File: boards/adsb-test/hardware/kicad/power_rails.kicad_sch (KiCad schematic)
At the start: 57 parts, among them SW401 POWER (slide), U411 TPS62933, U421 TPS62933, U430 TPS22917, U431 TPS22917, U432 TPS22917, U433 TPS22917

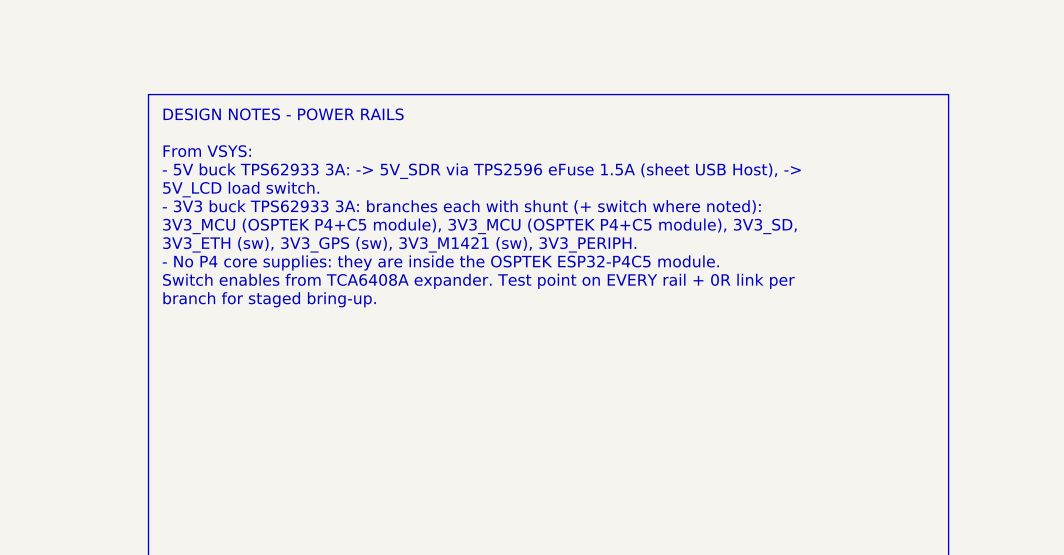
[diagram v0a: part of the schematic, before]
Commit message: ADSB_Test: net classes + diff-pair rules, USB pairs renamed _D_P/_D_N, U201 VSYS drawn at the bottom
Co-Authored-By: Claude Opus 5.5 <noreply@anthropic.com>
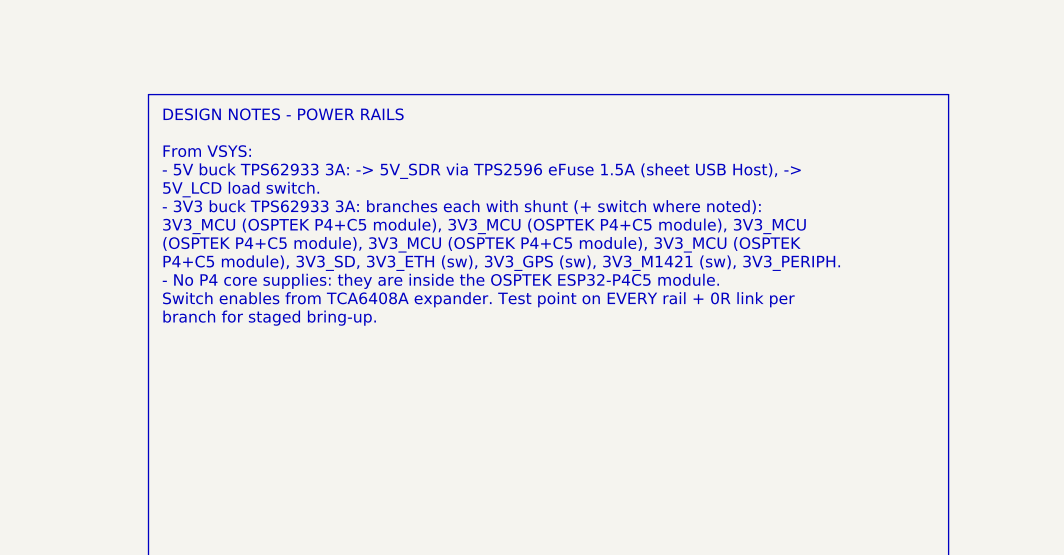
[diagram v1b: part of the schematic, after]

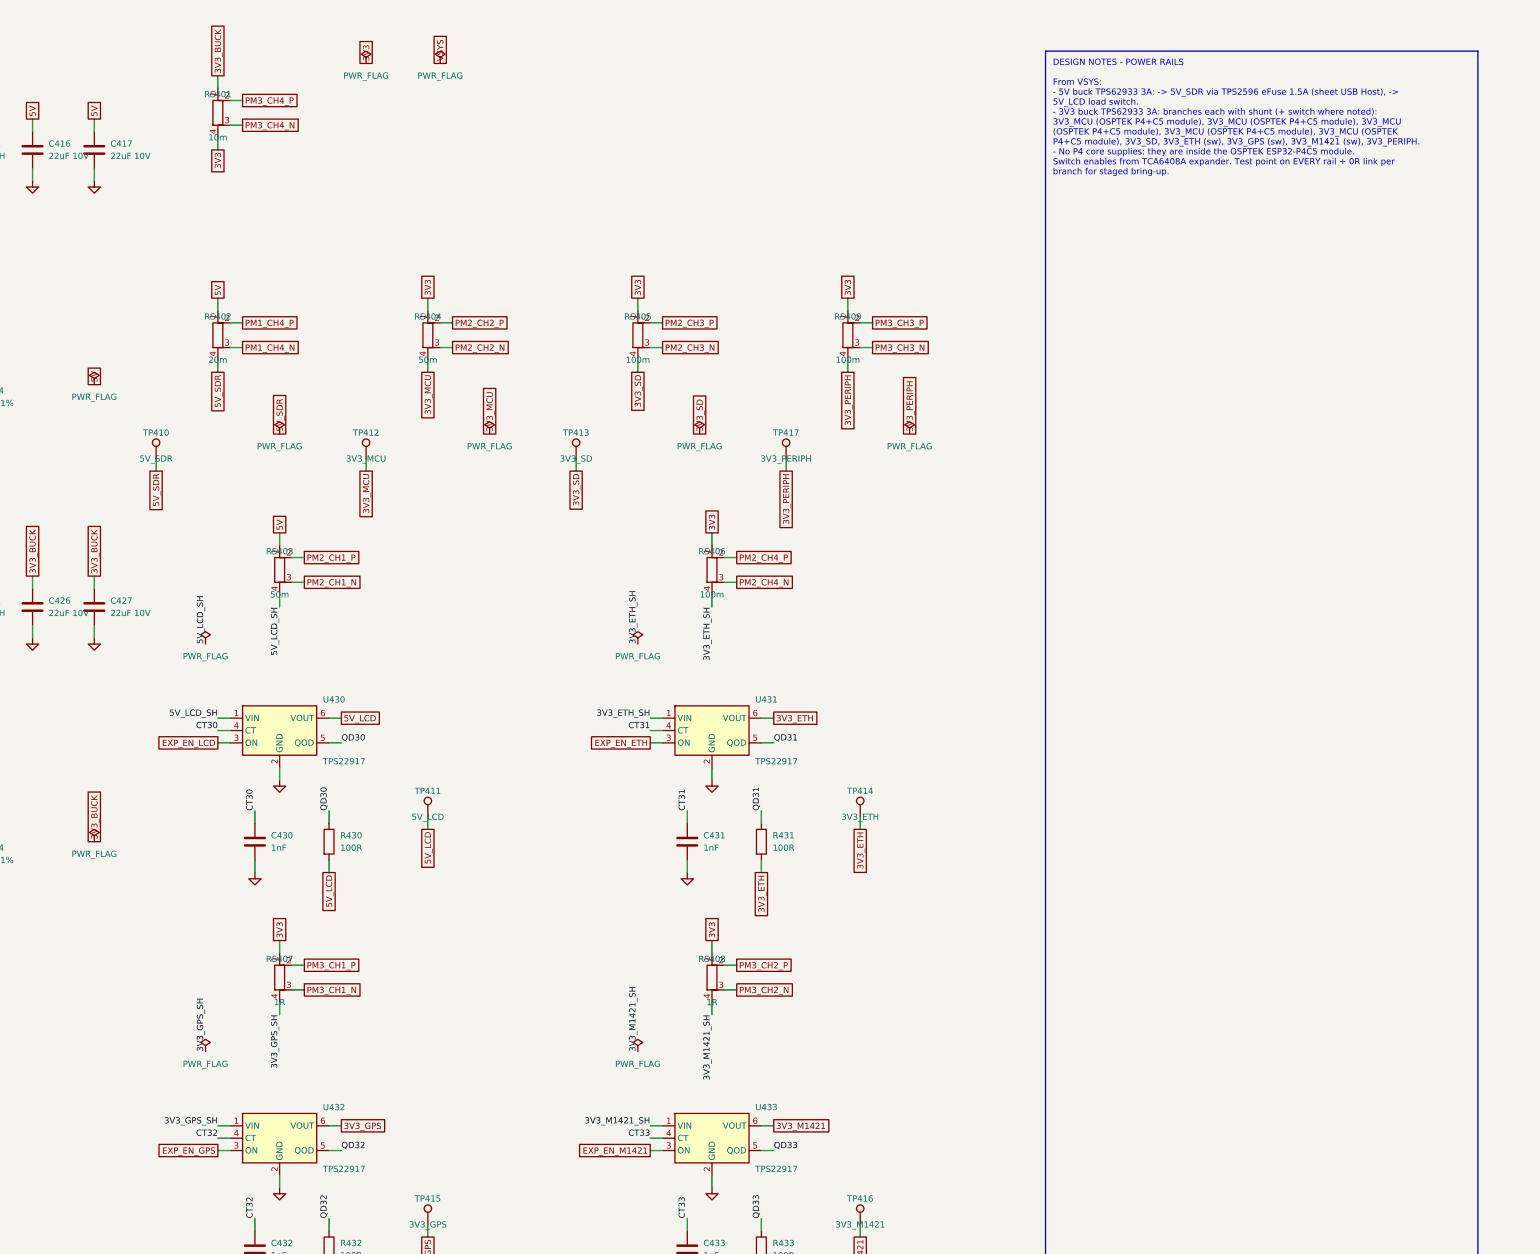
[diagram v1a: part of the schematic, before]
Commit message: ADSB_Test: User USB-C on its own sheet, RP2040 GPIO header + optional I2C, shunt/PWR_FLAG text fixed
Co-Authored-By: Claude Opus 5.5 <noreply@anthropic.com>
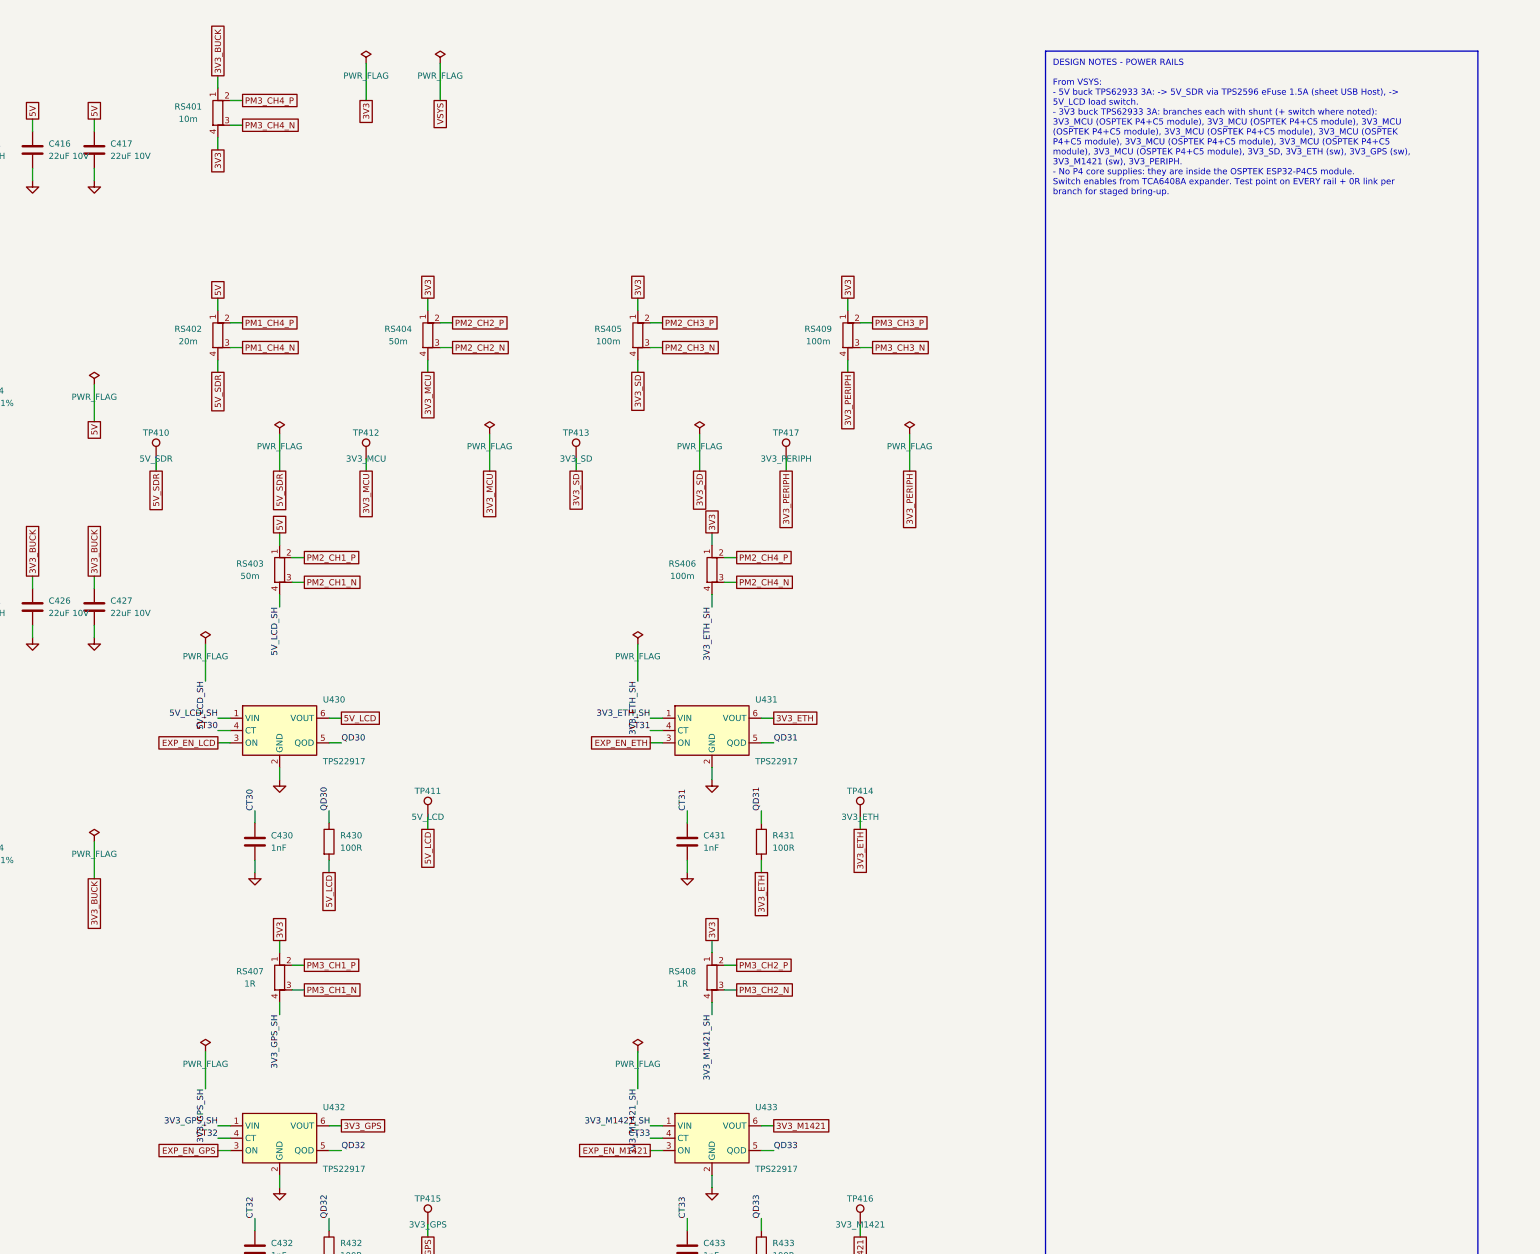
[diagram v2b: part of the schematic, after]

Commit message: ADSB_Test: Dev port split over three A3 sheets; old note boxes replaced with short current notes
Co-Authored-By: Claude Opus 5.5 <noreply@anthropic.com>
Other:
- note added: "RAILS: two TPS62933 bucks from VSYS (5 V and 3V3, 3 A each), shared PWR_EN with UVLO ~5.5 V. Every branch has a Kelvin shunt (PAC1954 channel on its sense labels) that doubles as a bring-up link. TPS22917 load switches on 5V_LCD, 3V3_ETH, 3V3_GPS, 3V3_M1421 (enabled from the TCA6408A). 3V3_MCU feeds the OSPTEK P4+C5 module."

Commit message: ADSB_Test: Kelvin shunt footprint, Wi-Fi RP-SMA on the top edge, PCB parity 0
- Shunts RS201-RS409: 4-pad R_Shunt_1206_Kelvin_HandSolder (net-tied sense
  pads) replaces the 2-pad 1206, which put the sense net on the load pad.
- Wi-Fi: module IPEX -> U.FL jumper -> J601 -> J602 RP-SMA on the top long
  edge, away from the 1090/978 and GNSS SMAs. BOM, datasheets, docs.
- gen_pcb: symbol fields and BOM flags copied to footprints, unconnected
  net names escaped; top-edge placement.

Co-Authored-By: Claude Opus 5.5 <noreply@anthropic.com>
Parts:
- RS401, RS402, RS403, RS404, RS405, RS406, RS407, RS408, RS409: footprint Resistor_SMD:R_1206_3216Metric_Pad1.30x1.75mm_HandSolder -> ADSB_Test:R_Shunt_1206_Kelvin_HandSolder; Check Kelvin-route pins 2/3 to the PAC1954 -> Route sense pads 2/3 to the PAC1954 as a pair

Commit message: ADSB_Test: current shunts resized for the PAC1954 100 mV range
Each shunt now gives ~40-75 mV at its rail's expected peak (several light
rails gave 2-20 mV): battery/VSYS 20m, 3V3 total 30m, 5V_SDR 50m, 3V3_SD
330m, 3V3_ETH 1R, m1421 and 3V3_PERIPH 2.2R. Full-scale currents on the
Power Monitor sheet, BOM updated, PCB regenerated (user's KiCad moves
captured into PLACE first; nothing moved, parity 0).

Co-Authored-By: Claude Opus 5.5 <noreply@anthropic.com>
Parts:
- RS401: value 10m -> 30m
- RS402: value 20m -> 50m
- RS405: value 100m -> 330m
- RS406: value 100m -> 1R
- RS408: value 1R -> 2.2R
- RS409: value 100m -> 2.2R
